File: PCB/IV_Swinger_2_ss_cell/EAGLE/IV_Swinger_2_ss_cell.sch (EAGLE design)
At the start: 34 parts

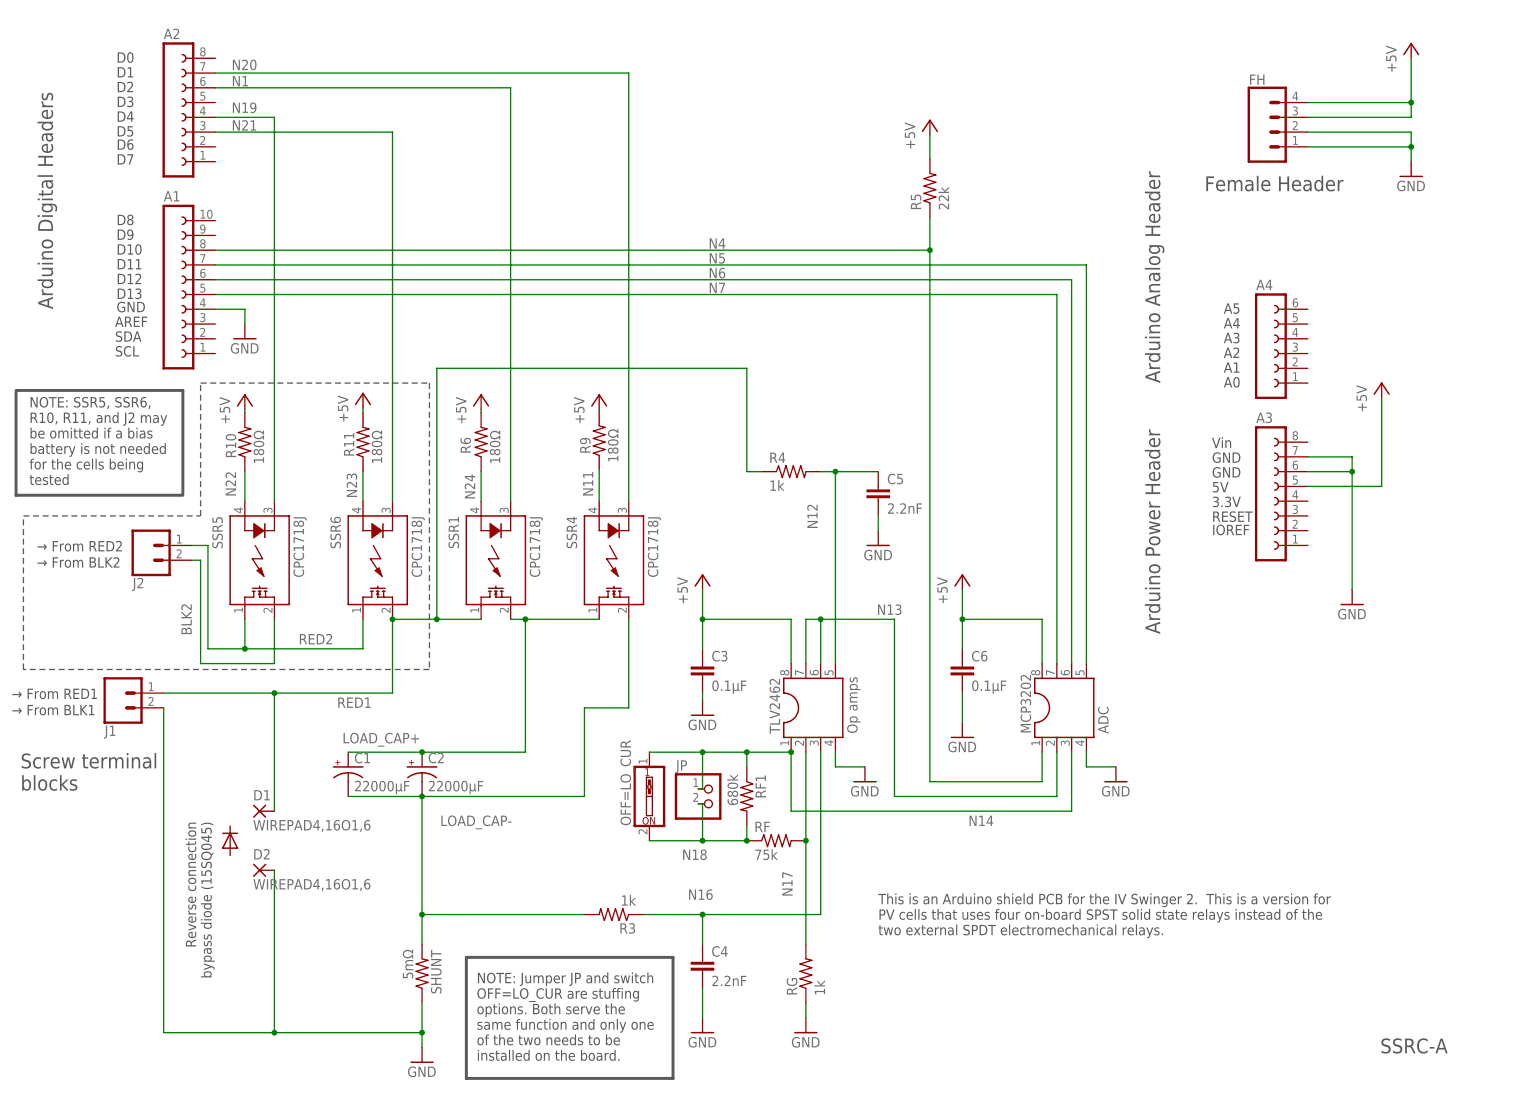
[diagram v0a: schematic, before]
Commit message: Change SSR4 from lin D1 to D8 on SSR cell version PCB (Issue #49)
This fixes Issue #49 on the SSR cell version PCB. SSR4 is now controlled by Arduino pin D8. This is now RevB (or SSRC-B) of this PCB.

This commit includes:
   EAGLE files, .sch and .brd
   Zip of the Rev_B Gerber files
   PDFs of the modified schematic, and the modified top and bottom images
   Updated GIFs that compare the SSR cell version with the other variants
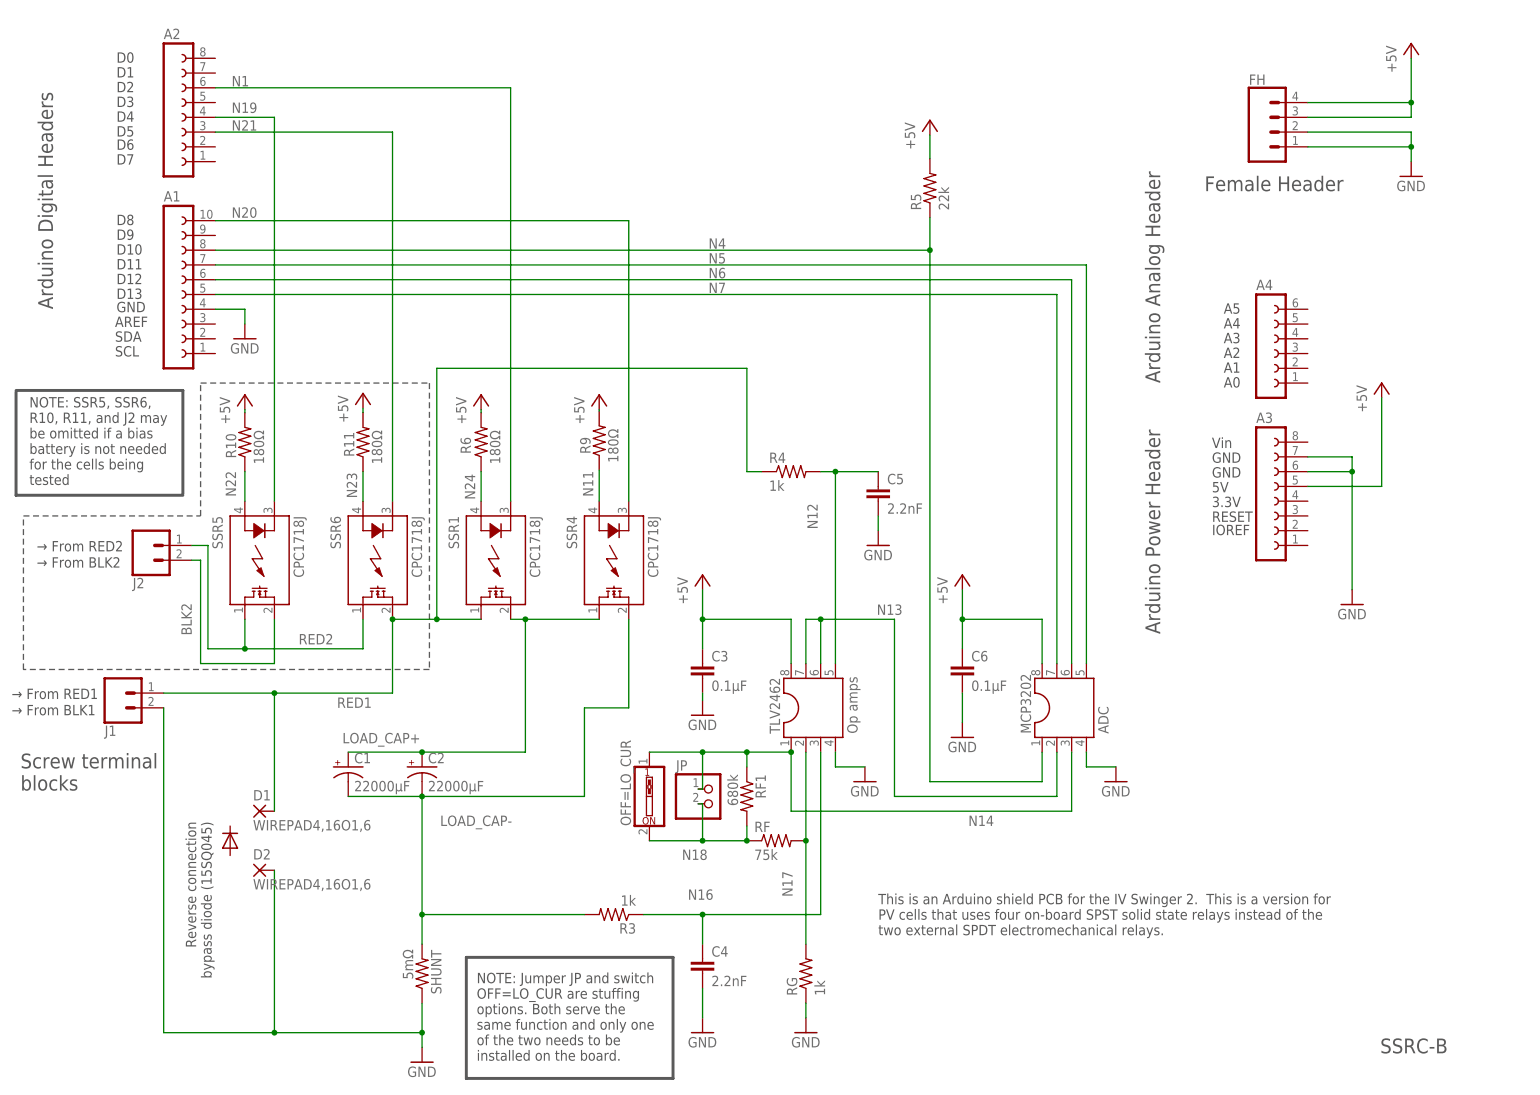
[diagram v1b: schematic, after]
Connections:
- net N20: now also A1.10; no longer A2.7
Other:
- note added: "SSRC-B"
- note removed: "SSRC-A"
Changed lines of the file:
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@@
 <text x="198.12" y="78.74" size="2.54" layer="97" rot="R90">Arduino Power Header</text>
 <text x="205.74" y="154.94" size="2.54" layer="97">Female Header</text>
-<text x="235.966" y="6.604" size="2.54" layer="97">SSRC-A</text>
+<text x="235.966" y="6.604" size="2.54" layer="97">SSRC-B</text>
 <text x="149.606" y="26.924" size="1.778" layer="97">This is an Arduino shield PCB for the IV Swinger 2.  This is a version for
 PV cells that uses four on-board SPST solid state relays instead of the
@@
 <segment>
 <pinref part="SSR4" gate="G$1" pin="K"/>
-<wire x1="106.68" y1="101.6" x2="106.68" y2="175.26" width="0.1524" layer="91"/>
-<label x="38.354" y="175.768" size="1.778" layer="95"/>
-<pinref part="A2" gate="G$1" pin="7"/>
-<wire x1="35.56" y1="175.26" x2="106.68" y2="175.26" width="0.1524" layer="91"/>
-</segment>
-</net>
+<label x="38.354" y="150.368" size="1.778" layer="95"/>
+<pinref part="A1" gate="G$1" pin="10"/>
+<wire x1="35.56" y1="149.86" x2="106.68" y2="149.86" width="0.1524" layer="91"/>
+<wire x1="106.68" y1="149.86" x2="106.68" y2="101.6" width="0.1524" layer="91"/>
+</segment>
+</net>
